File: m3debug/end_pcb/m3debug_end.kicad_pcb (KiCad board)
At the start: 2 copper layers, 46 x 26 mm, 9 parts, among them J1 WEST TOP, J2 EAST TOP, J3 WEST BOT, J4 EAST BOT, J5 CONN_01x10, J6 CONN_01x10, J7 CONN_01x10, J8 CONN_01x10

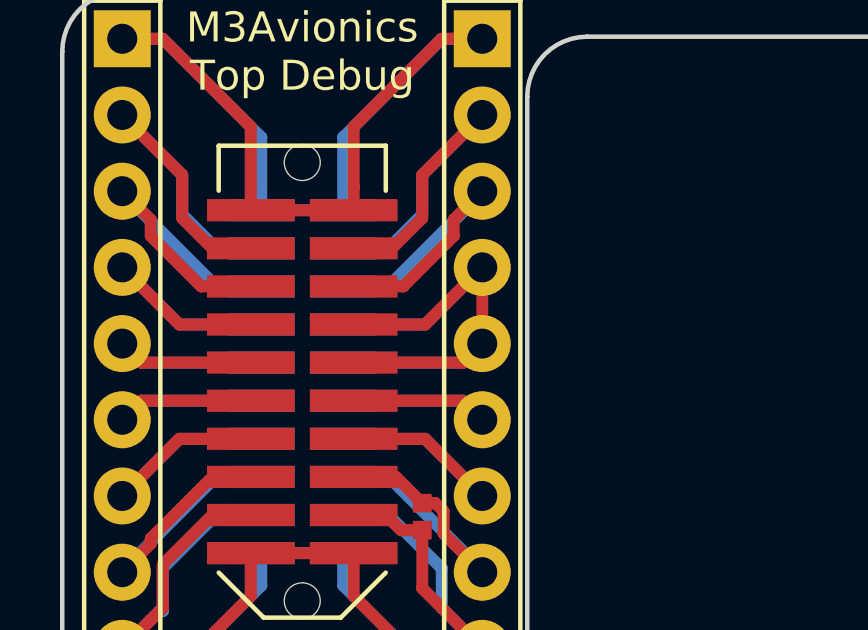
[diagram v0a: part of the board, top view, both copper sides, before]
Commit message: add cusf logo on silk
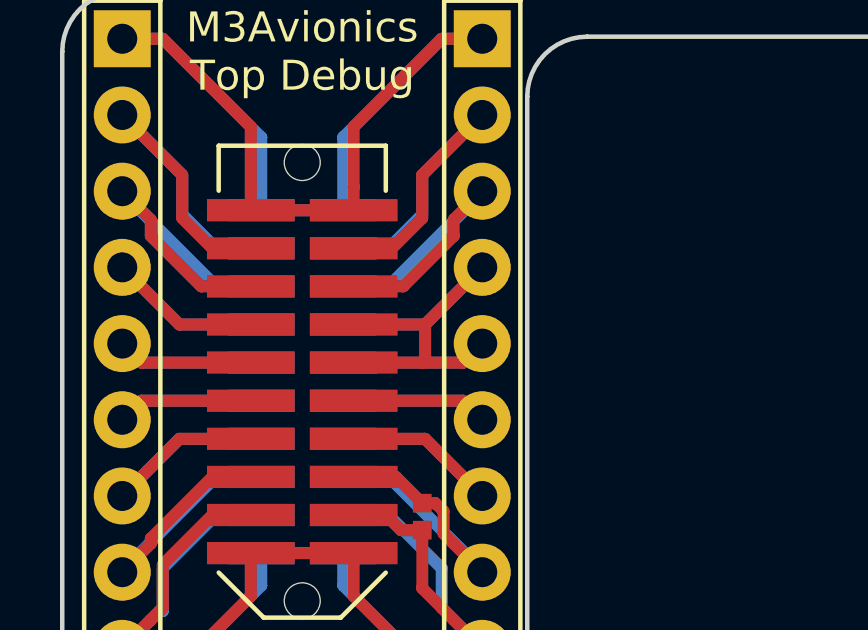
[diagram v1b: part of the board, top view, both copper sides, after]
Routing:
- net /JTDI: track 22.5 -> 21.3 mm
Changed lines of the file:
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@@
-(kicad_pcb (version 4) (host pcbnew 0.201512291232+6408~40~ubuntu14.04.1-stable)
+(kicad_pcb (version 4) (host pcbnew 0.201601071449+6428~40~ubuntu14.04.1-stable)
   (general
     (links 93)
-    (no_connects 93)
-    (area 76.924999 86.924999 123.075001 113.075001)
+    (no_connects 3)
+    (area 75.655 86.844999 124.195 113.155001)
     (thickness 1.6)
     (drawings 18)
-    (tracks 245)
+    (tracks 247)
     (zones 0)
     (modules 9)
@@
     (visible_elements FFFFFF7F)
     (pcbplotparams
-      (layerselection 0x00030_ffffffff)
-      (usegerberextensions false)
+      (layerselection 0x010f0_ffffffff)
+      (usegerberextensions true)
       (excludeedgelayer true)
       (linewidth 0.100000)
@@
       (psnegative false)
       (psa4output false)
-      (plotreference true)
-      (plotvalue true)
+      (plotreference false)
+      (plotvalue false)
       (plotinvisibletext false)
       (padsonsilk false)
-      (subtractmaskfromsilk false)
+      (subtractmaskfromsilk true)
       (outputformat 1)
       (mirror false)
-      (drillshape 1)
+      (drillshape 0)
       (scaleselection 1)
-      (outputdirectory ""))
+      (outputdirectory gerbers/))
   )
   (net 0 "")
@@
   (segment (start 83.285 98.095) (end 80.905 98.095) (width 0.4) (layer F.Cu) (net 6))
   (segment (start 80.905 98.095) (end 79 96.19) (width 0.4) (layer F.Cu) (net 6))
-  (segment (start 91 96.19) (end 91 98.73) (width 0.4) (layer F.Cu) (net 7))
-  (segment (start 86.715 99.365) (end 90.365 99.365) (width 0.4) (layer F.Cu) (net 7))
+  (segment (start 86.715 99.365) (end 89 99.365) (width 0.4) (layer F.Cu) (net 7))
+  (segment (start 89 99.365) (end 90.365 99.365) (width 0.4) (layer F.Cu) (net 7))
+  (segment (start 89.095 98.095) (end 89.095 99.27) (width 0.4) (layer F.Cu) (net 7))
+  (segment (start 89.095 99.27) (end 89 99.365) (width 0.4) (layer F.Cu) (net 7))
   (segment (start 86.365 98.095) (end 89.095 98.095) (width 0.4) (layer B.Cu) (net 7))
   (segment (start 89.095 98.095) (end 91 96.19) (width 0.4) (layer B.Cu) (net 7))
